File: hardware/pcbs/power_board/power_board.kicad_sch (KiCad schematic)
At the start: 4 parts

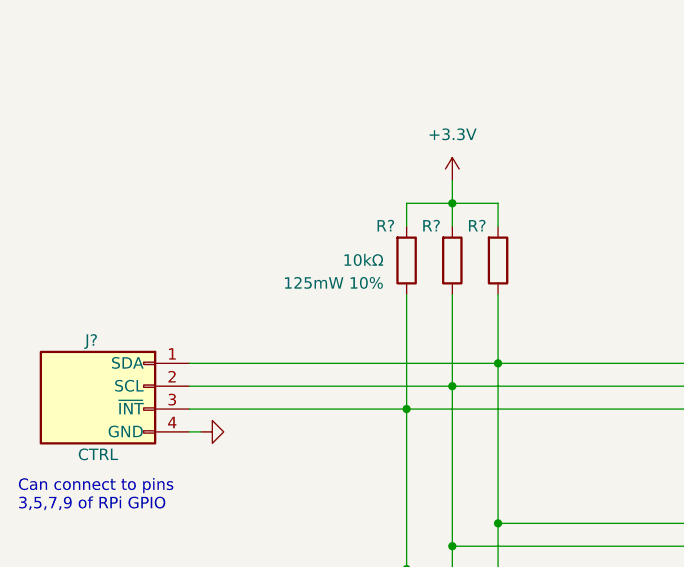
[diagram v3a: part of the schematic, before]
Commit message: power_board: minor fixes to shematic
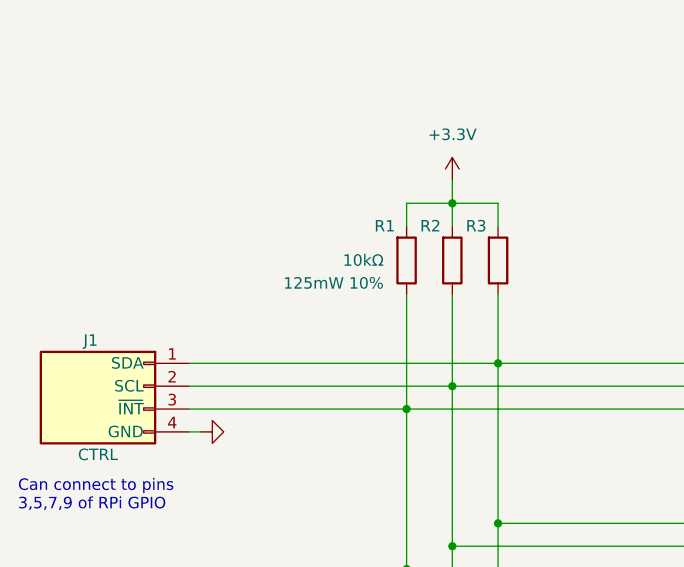
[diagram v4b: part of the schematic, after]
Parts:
- gave numbers to parts that had none: 4
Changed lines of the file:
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@@
   (symbol (lib_id "conn:Conn_01x04") (at 67.31 86.36 0) (mirror y) (unit 1)
     (in_bom yes) (on_board yes) (dnp no)
-    (property "Reference" "J?" (at 62.23 81.28 0)
+    (property "Reference" "J1" (at 62.23 81.28 0)
       (effects (font (size 1.27 1.27)) (justify left))
     )
@@
       (project "power_board"
         (path "/4b166175-80a4-48c6-994d-6e62a6160b87"
-          (reference "J?") (unit 1)
+          (reference "J1") (unit 1)
         )
       )
@@
   (symbol (lib_id "Device:R") (at 106.68 72.39 0) (mirror x) (unit 1)
     (in_bom yes) (on_board yes) (dnp no)
-    (property "Reference" "R?" (at 105.41 68.58 0)
+    (property "Reference" "R3" (at 105.41 68.58 0)
       (effects (font (size 1.27 1.27)) (justify right))
     )
@@
       (project "power_board"
         (path "/4b166175-80a4-48c6-994d-6e62a6160b87"
-          (reference "R?") (unit 1)
+          (reference "R3") (unit 1)
         )
       )
@@
   (symbol (lib_id "Device:R") (at 96.52 72.39 0) (mirror x) (unit 1)
     (in_bom yes) (on_board yes) (dnp no)
-    (property "Reference" "R?" (at 95.25 68.58 0)
+    (property "Reference" "R1" (at 95.25 68.58 0)
       (effects (font (size 1.27 1.27)) (justify right))
     )
@@
       (project "power_board"
         (path "/4b166175-80a4-48c6-994d-6e62a6160b87"
-          (reference "R?") (unit 1)
+          (reference "R1") (unit 1)
         )
       )
@@
   (symbol (lib_id "power:+12V") (at 173.99 48.26 270) (unit 1)
     (in_bom yes) (on_board yes) (dnp no)
-    (property "Reference" "#PWR082" (at 170.18 48.26 0)
+    (property "Reference" "#PWR03" (at 170.18 48.26 0)
       (effects (font (size 1.27 1.27)) hide)
     )
@@
       (project "power_board"
         (path "/4b166175-80a4-48c6-994d-6e62a6160b87"
-          (reference "#PWR082") (unit 1)
+          (reference "#PWR03") (unit 1)
         )
       )
@@
   (symbol (lib_id "power:+3.3V") (at 173.99 53.34 270) (unit 1)
     (in_bom yes) (on_board yes) (dnp no) (fields_autoplaced)
-    (property "Reference" "#PWR084" (at 170.18 53.34 0)
+    (property "Reference" "#PWR05" (at 170.18 53.34 0)
       (effects (font (size 1.27 1.27)) hide)
     )
@@
       (project "power_board"
         (path "/4b166175-80a4-48c6-994d-6e62a6160b87"
-          (reference "#PWR084") (unit 1)
+          (reference "#PWR05") (unit 1)
         )
       )
@@
   (symbol (lib_id "power:+5V") (at 173.99 50.8 270) (unit 1)
     (in_bom yes) (on_board yes) (dnp no) (fields_autoplaced)
-    (property "Reference" "#PWR083" (at 170.18 50.8 0)
+    (property "Reference" "#PWR04" (at 170.18 50.8 0)
       (effects (font (size 1.27 1.27)) hide)
     )
@@
       (project "power_board"
         (path "/4b166175-80a4-48c6-994d-6e62a6160b87"
-          (reference "#PWR083") (unit 1)
+          (reference "#PWR04") (unit 1)
         )
       )
@@
   (symbol (lib_id "Device:R") (at 101.6 72.39 0) (mirror x) (unit 1)
     (in_bom yes) (on_board yes) (dnp no)
-    (property "Reference" "R?" (at 100.33 68.58 0)
+    (property "Reference" "R2" (at 100.33 68.58 0)
       (effects (font (size 1.27 1.27)) (justify right))
     )
@@
       (project "power_board"
         (path "/4b166175-80a4-48c6-994d-6e62a6160b87"
-          (reference "R?") (unit 1)
+          (reference "R2") (unit 1)
         )
       )
@@
   (symbol (lib_id "power:+3.3V") (at 101.6 63.5 0) (unit 1)
     (in_bom yes) (on_board yes) (dnp no) (fields_autoplaced)
-    (property "Reference" "#PWR066" (at 101.6 67.31 0)
+    (property "Reference" "#PWR02" (at 101.6 67.31 0)
       (effects (font (size 1.27 1.27)) hide)
     )
@@
       (project "power_board"
         (path "/4b166175-80a4-48c6-994d-6e62a6160b87"
-          (reference "#PWR066") (unit 1)
+          (reference "#PWR02") (unit 1)
         )
       )
@@
   (symbol (lib_id "power:GND") (at 73.66 91.44 90) (unit 1)
     (in_bom yes) (on_board yes) (dnp no) (fields_autoplaced)
-    (property "Reference" "#PWR065" (at 80.01 91.44 0)
+    (property "Reference" "#PWR01" (at 80.01 91.44 0)
       (effects (font (size 1.27 1.27)) hide)
     )
@@
       (project "power_board"
         (path "/4b166175-80a4-48c6-994d-6e62a6160b87"
-          (reference "#PWR065") (unit 1)
-        )
-      )
+          (reference "#PWR01") (unit 1)
+        )
+      )

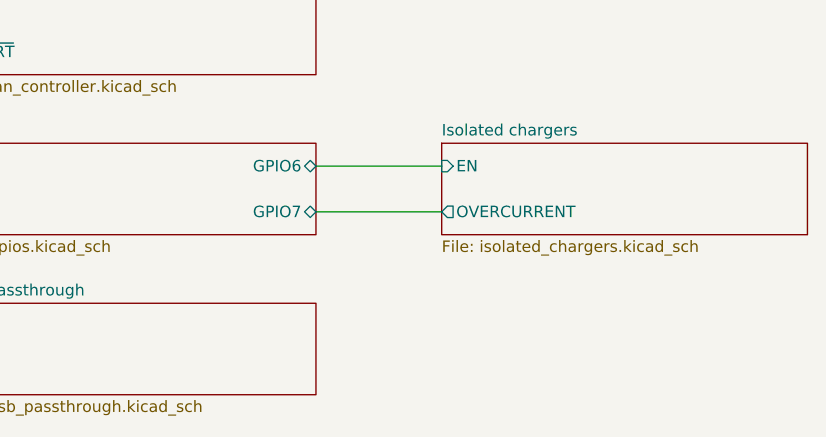
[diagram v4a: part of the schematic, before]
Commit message: power_board: connect power led to SBC's usb and fix inductor values
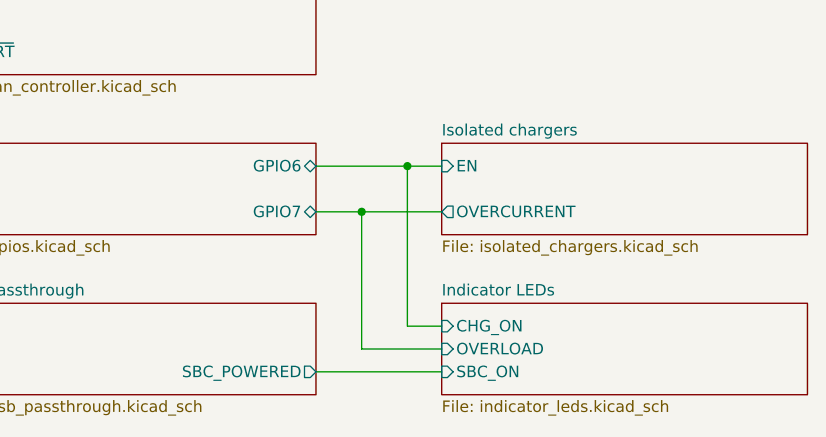
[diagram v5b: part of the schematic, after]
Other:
- added sheet Indicator LEDs (indicator_leds.kicad_sch)
- sheet USB Passthrough ports: added SBC_POWERED; removed none
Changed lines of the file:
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@@
   (junction (at 101.6 104.14) (diameter 0) (color 0 0 0 0)
   )
+  (junction (at 181.61 119.38) (diameter 0) (color 0 0 0 0)
+  )
   (junction (at 96.52 88.9) (diameter 0) (color 0 0 0 0)
   )
@@
   (junction (at 96.52 106.68) (diameter 0) (color 0 0 0 0)
   )
+  (junction (at 176.53 124.46) (diameter 0) (color 0 0 0 0)
+  )
   (junction (at 106.68 83.82) (diameter 0) (color 0 0 0 0)
   )
   (junction (at 106.68 101.6) (diameter 0) (color 0 0 0 0)
   )
-  (wire (pts (xy 171.45 119.38) (xy 185.42 119.38))
+  (wire (pts (xy 171.45 119.38) (xy 181.61 119.38))
+    (stroke (width 0) (type default))
+  )
+  (wire (pts (xy 185.42 139.7) (xy 176.53 139.7))
     (stroke (width 0) (type default))
   )
@@
     (stroke (width 0) (type default))
   )
+  (wire (pts (xy 171.45 142.24) (xy 185.42 142.24))
+    (stroke (width 0) (type default))
+  )
   (wire (pts (xy 101.6 66.04) (xy 106.68 66.04))
     (stroke (width 0) (type default))
@@
     (stroke (width 0) (type default))
   )
-  (wire (pts (xy 171.45 124.46) (xy 185.42 124.46))
+  (wire (pts (xy 171.45 124.46) (xy 176.53 124.46))
     (stroke (width 0) (type default))
   )
@@
     (stroke (width 0) (type default))
   )
+  (wire (pts (xy 176.53 139.7) (xy 176.53 124.46))
+    (stroke (width 0) (type default))
+  )
+  (wire (pts (xy 176.53 124.46) (xy 185.42 124.46))
+    (stroke (width 0) (type default))
+  )
   (wire (pts (xy 72.39 91.44) (xy 73.66 91.44))
     (stroke (width 0) (type default))
@@
     (stroke (width 0) (type default))
   )
+  (wire (pts (xy 185.42 137.16) (xy 181.61 137.16))
+    (stroke (width 0) (type default))
+  )
   (wire (pts (xy 96.52 88.9) (xy 130.81 88.9))
     (stroke (width 0) (type default))
@@
     (stroke (width 0) (type default))
   )
+  (wire (pts (xy 181.61 119.38) (xy 185.42 119.38))
+    (stroke (width 0) (type default))
+  )
   (wire (pts (xy 106.68 83.82) (xy 130.81 83.82))
     (stroke (width 0) (type default))
@@
   )
   (wire (pts (xy 96.52 106.68) (xy 130.81 106.68))
+    (stroke (width 0) (type default))
+  )
+  (wire (pts (xy 181.61 137.16) (xy 181.61 119.38))
     (stroke (width 0) (type default))
   )
@@
       (effects (font (size 1.27 1.27)) (justify left top))
     )
+    (pin "SBC_POWERED" output (at 171.45 142.24 0)
+      (effects (font (size 1.27 1.27)) (justify right))
+    )
     (instances
       (project "power_board"
@@
       )
     )
+  )
+  (sheet (at 185.42 134.62) (size 40.64 10.16) (fields_autoplaced)
+    (stroke (width 0.1524) (type solid))
+    (fill (color 0 0 0 0.0000))
+    (property "Sheetname" "Indicator LEDs" (at 185.42 133.9084 0)
+      (effects (font (size 1.27 1.27)) (justify left bottom))
+    )
+    (property "Sheetfile" "indicator_leds.kicad_sch" (at 185.42 145.3646 0)
+      (effects (font (size 1.27 1.27)) (justify left top))
+    )
+    (pin "OVERLOAD" input (at 185.42 139.7 180)
+      (effects (font (size 1.27 1.27)) (justify left))
+    )
+    (pin "SBC_ON" input (at 185.42 142.24 180)
+      (effects (font (size 1.27 1.27)) (justify left))
+    )
+    (pin "CHG_ON" input (at 185.42 137.16 180)
+      (effects (font (size 1.27 1.27)) (justify left))
+    )
+    (instances
+      (project "power_board"
+        (path "/4b166175-80a4-48c6-994d-6e62a6160b87" (page "12"))
+      )
+    )

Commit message: power_board: finalise all footprints
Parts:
- J1: Shop (none) -> https://store.comet.bg/Catalogue/Product/17821/
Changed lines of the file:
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@@
       (effects (font (size 1.27 1.27)) (justify left))
+    )
+    (property "Shop" "https://store.comet.bg/Catalogue/Product/17821/" (at 67.31 86.36 0)
+      (effects (font (size 1.27 1.27)) hide)
     )
     (pin "4")

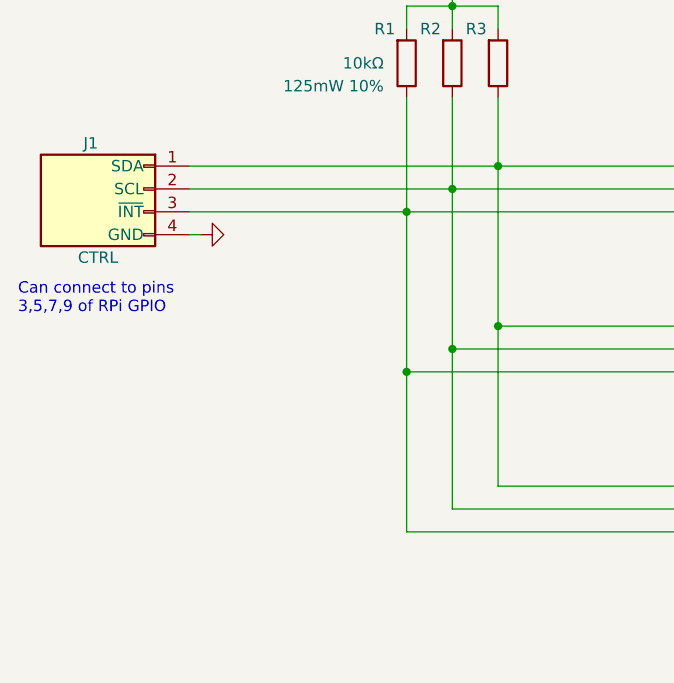
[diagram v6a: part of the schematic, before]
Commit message: power_board: a couple of extra connectors
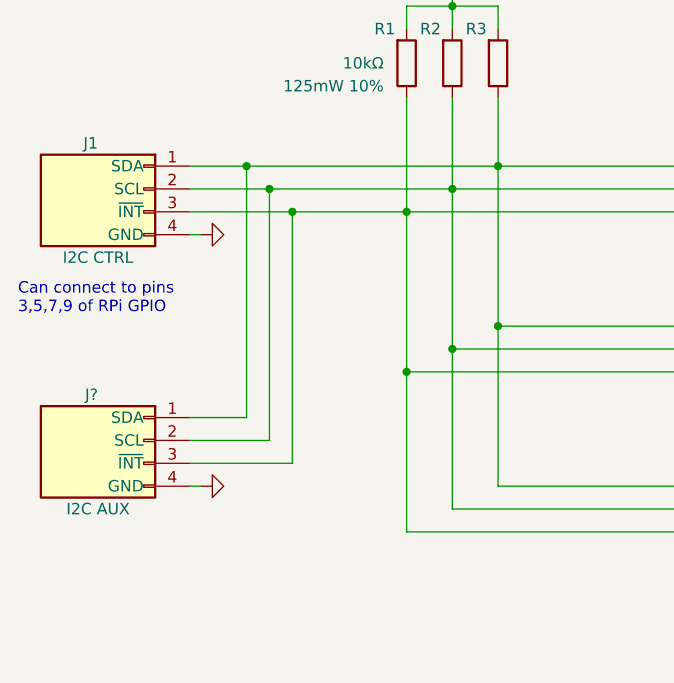
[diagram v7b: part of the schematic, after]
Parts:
- added J?: Header_01x04, conn:PinHeader_1x04_P2.54mm_Vertical, symbol conn:Conn_01x04
- J1: Purpose CTRL -> I2C CTRL
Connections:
- net Fan Controller/SCL: now also J?.2 (Pin_2)
- net Fan Controller/SDA: now also J?.1 (Pin_1)
- net Fan Controller/~{ALERT}: now also J?.3 (Pin_3)
- net GND: now also J?.4 (Pin_4)
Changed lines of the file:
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@@
   (junction (at 101.6 104.14) (diameter 0) (color 0 0 0 0)
   )
+  (junction (at 81.28 86.36) (diameter 0) (color 0 0 0 0)
+  )
   (junction (at 181.61 119.38) (diameter 0) (color 0 0 0 0)
   )
@@
   (junction (at 101.6 66.04) (diameter 0) (color 0 0 0 0)
   )
+  (junction (at 83.82 88.9) (diameter 0) (color 0 0 0 0)
+  )
   (junction (at 96.52 106.68) (diameter 0) (color 0 0 0 0)
   )
@@
   (junction (at 106.68 83.82) (diameter 0) (color 0 0 0 0)
   )
+  (junction (at 78.74 83.82) (diameter 0) (color 0 0 0 0)
+  )
   (junction (at 106.68 101.6) (diameter 0) (color 0 0 0 0)
   )
+  (wire (pts (xy 81.28 86.36) (xy 101.6 86.36))
+    (stroke (width 0) (type default))
+  )
   (wire (pts (xy 171.45 119.38) (xy 181.61 119.38))
     (stroke (width 0) (type default))
@@
     (stroke (width 0) (type default))
   )
-  (wire (pts (xy 72.39 83.82) (xy 106.68 83.82))
+  (wire (pts (xy 72.39 83.82) (xy 78.74 83.82))
     (stroke (width 0) (type default))
   )
@@
     (stroke (width 0) (type default))
   )
+  (wire (pts (xy 72.39 116.84) (xy 83.82 116.84))
+    (stroke (width 0) (type default))
+  )
+  (wire (pts (xy 72.39 119.38) (xy 73.66 119.38))
+    (stroke (width 0) (type default))
+  )
   (wire (pts (xy 96.52 76.2) (xy 96.52 88.9))
     (stroke (width 0) (type default))
@@
     (stroke (width 0) (type default))
   )
-  (wire (pts (xy 72.39 86.36) (xy 101.6 86.36))
+  (wire (pts (xy 72.39 86.36) (xy 81.28 86.36))
     (stroke (width 0) (type default))
   )
@@
     (stroke (width 0) (type default))
   )
+  (wire (pts (xy 78.74 111.76) (xy 78.74 83.82))
+    (stroke (width 0) (type default))
+  )
   (wire (pts (xy 176.53 139.7) (xy 176.53 124.46))
     (stroke (width 0) (type default))
   )
+  (wire (pts (xy 72.39 111.76) (xy 78.74 111.76))
+    (stroke (width 0) (type default))
+  )
   (wire (pts (xy 176.53 124.46) (xy 185.42 124.46))
     (stroke (width 0) (type default))
@@
     (stroke (width 0) (type default))
   )
+  (wire (pts (xy 72.39 114.3) (xy 81.28 114.3))
+    (stroke (width 0) (type default))
+  )
   (wire (pts (xy 101.6 63.5) (xy 101.6 66.04))
     (stroke (width 0) (type default))
   )
+  (wire (pts (xy 78.74 83.82) (xy 106.68 83.82))
+    (stroke (width 0) (type default))
+  )
   (wire (pts (xy 101.6 104.14) (xy 130.81 104.14))
     (stroke (width 0) (type default))
   )
+  (wire (pts (xy 81.28 114.3) (xy 81.28 86.36))
+    (stroke (width 0) (type default))
+  )
   (wire (pts (xy 185.42 137.16) (xy 181.61 137.16))
     (stroke (width 0) (type default))
@@
     (stroke (width 0) (type default))
   )
+  (wire (pts (xy 83.82 88.9) (xy 96.52 88.9))
+    (stroke (width 0) (type default))
+  )
+  (wire (pts (xy 83.82 116.84) (xy 83.82 88.9))
+    (stroke (width 0) (type default))
+  )
   (wire (pts (xy 106.68 83.82) (xy 130.81 83.82))
     (stroke (width 0) (type default))
@@
     (stroke (width 0) (type default))
   )
-  (wire (pts (xy 72.39 88.9) (xy 96.52 88.9))
+  (wire (pts (xy 72.39 88.9) (xy 83.82 88.9))
     (stroke (width 0) (type default))
   )
@@
       (effects (font (size 1.27 1.27)) hide)
     )
-    (property "Purpose" "CTRL" (at 62.23 93.98 0)
+    (property "Purpose" "I2C CTRL" (at 62.23 93.98 0)
       (effects (font (size 1.27 1.27)))
     )
@@
     )
   )
+  (symbol (lib_id "conn:Conn_01x04") (at 67.31 114.3 0) (mirror y) (unit 1)
+    (in_bom yes) (on_board yes) (dnp no)
+    (property "Reference" "J?" (at 62.23 109.22 0)
+      (effects (font (size 1.27 1.27)) (justify left))
+    )
+    (property "Value" "Header_01x04" (at 62.23 121.92 0)
+      (effects (font (size 1.27 1.27)) hide)
+    )
+    (property "Footprint" "conn:PinHeader_1x04_P2.54mm_Vertical" (at 67.31 114.3 0)
+      (effects (font (size 1.27 1.27)) hide)
+    )
+    (property "Datasheet" "~" (at 67.31 114.3 0)
+      (effects (font (size 1.27 1.27)) hide)
+    )
+    (property "Purpose" "I2C AUX" (at 62.23 121.92 0)
+      (effects (font (size 1.27 1.27)))
+    )
+    (property "Purpose Pin1" "SDA" (at 67.31 111.76 0)
+      (effects (font (size 1.27 1.27)) (justify left))
+    )
+    (property "Purpose Pin2" "SCL" (at 67.31 114.3 0)
+      (effects (font (size 1.27 1.27)) (justify left))
+    )
+    (property "Purpose Pin3" "~{INT}" (at 67.31 116.84 0)
+      (effects (font (size 1.27 1.27)) (justify left))
+    )
+    (property "Purpose Pin4" "GND" (at 67.31 119.38 0)
+      (effects (font (size 1.27 1.27)) (justify left))
+    )
+    (property "Shop" "https://store.comet.bg/Catalogue/Product/17821/" (at 67.31 114.3 0)
+      (effects (font (size 1.27 1.27)) hide)
+    )
+    (pin "4")
+    (pin "1")
+    (pin "2")
+    (pin "3")
+    (instances
+      (project "power_board"
+        (path "/4b166175-80a4-48c6-994d-6e62a6160b87"
+          (reference "J?") (unit 1)
+        )
+      )
+    )
+  )
   (symbol (lib_id "Device:R") (at 101.6 72.39 0) (mirror x) (unit 1)
     (in_bom yes) (on_board yes) (dnp no)
@@
         )
       )
+    )
+  )
+  (symbol (lib_id "power:GND") (at 73.66 119.38 90) (unit 1)
+    (in_bom yes) (on_board yes) (dnp no) (fields_autoplaced)
+    (property "Reference" "#PWR0105" (at 80.01 119.38 0)
+      (effects (font (size 1.27 1.27)) hide)
+    )
+    (property "Value" "GND" (at 78.74 119.38 0)
+      (effects (font (size 1.27 1.27)) hide)
+    )
+    (property "Footprint" "" (at 73.66 119.38 0)
+      (effects (font (size 1.27 1.27)) hide)
+    )
+    (property "Datasheet" "" (at 73.66 119.38 0)
+      (effects (font (size 1.27 1.27)) hide)
+    )
+    (pin "1")
+    (instances
+      (project "power_board"
+        (path "/4b166175-80a4-48c6-994d-6e62a6160b87"
+          (reference "#PWR0105") (unit 1)
+        )
+      )
